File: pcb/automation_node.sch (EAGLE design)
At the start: 27 parts, among them IC1 POWER_FET, IC2 POWER_FET, IC3 POWER_FET, IC4 POWER_FET, IC5 POWER_FET, IC6 FEATHER-ESP32, J1 POWER-VIAS, J2 POWER-VIAS, J3 POWER-VIAS, J4 POWER-VIAS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

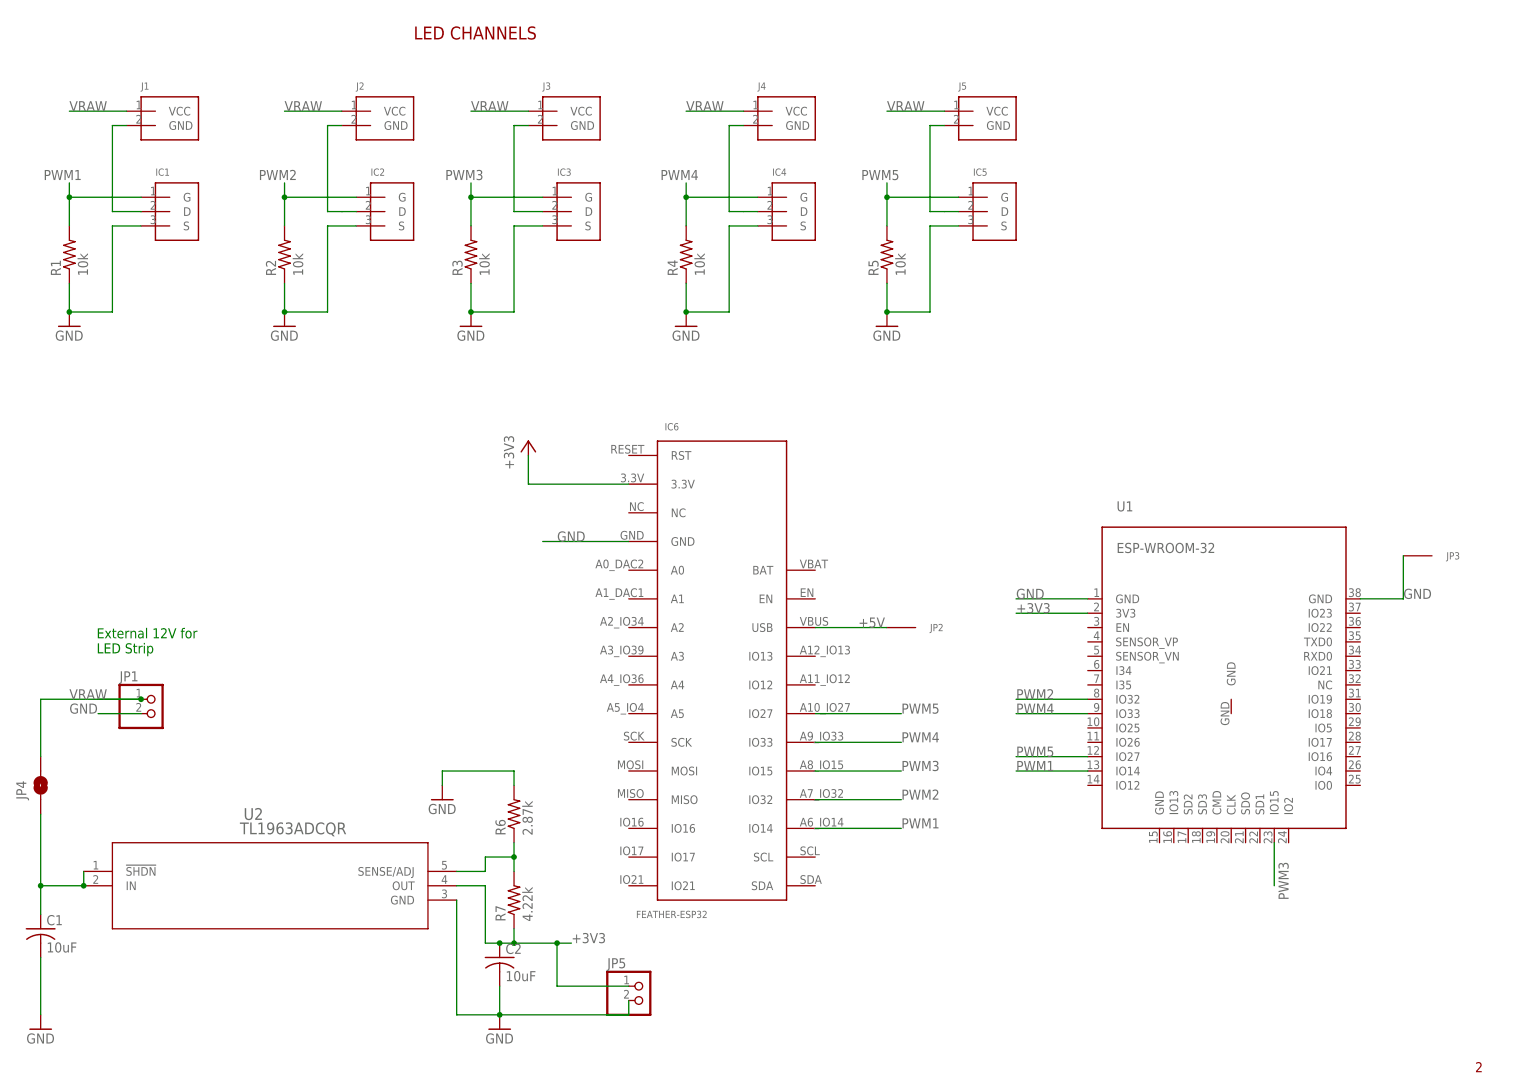
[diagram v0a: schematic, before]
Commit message: added RFM69, finished routing all but RFM69
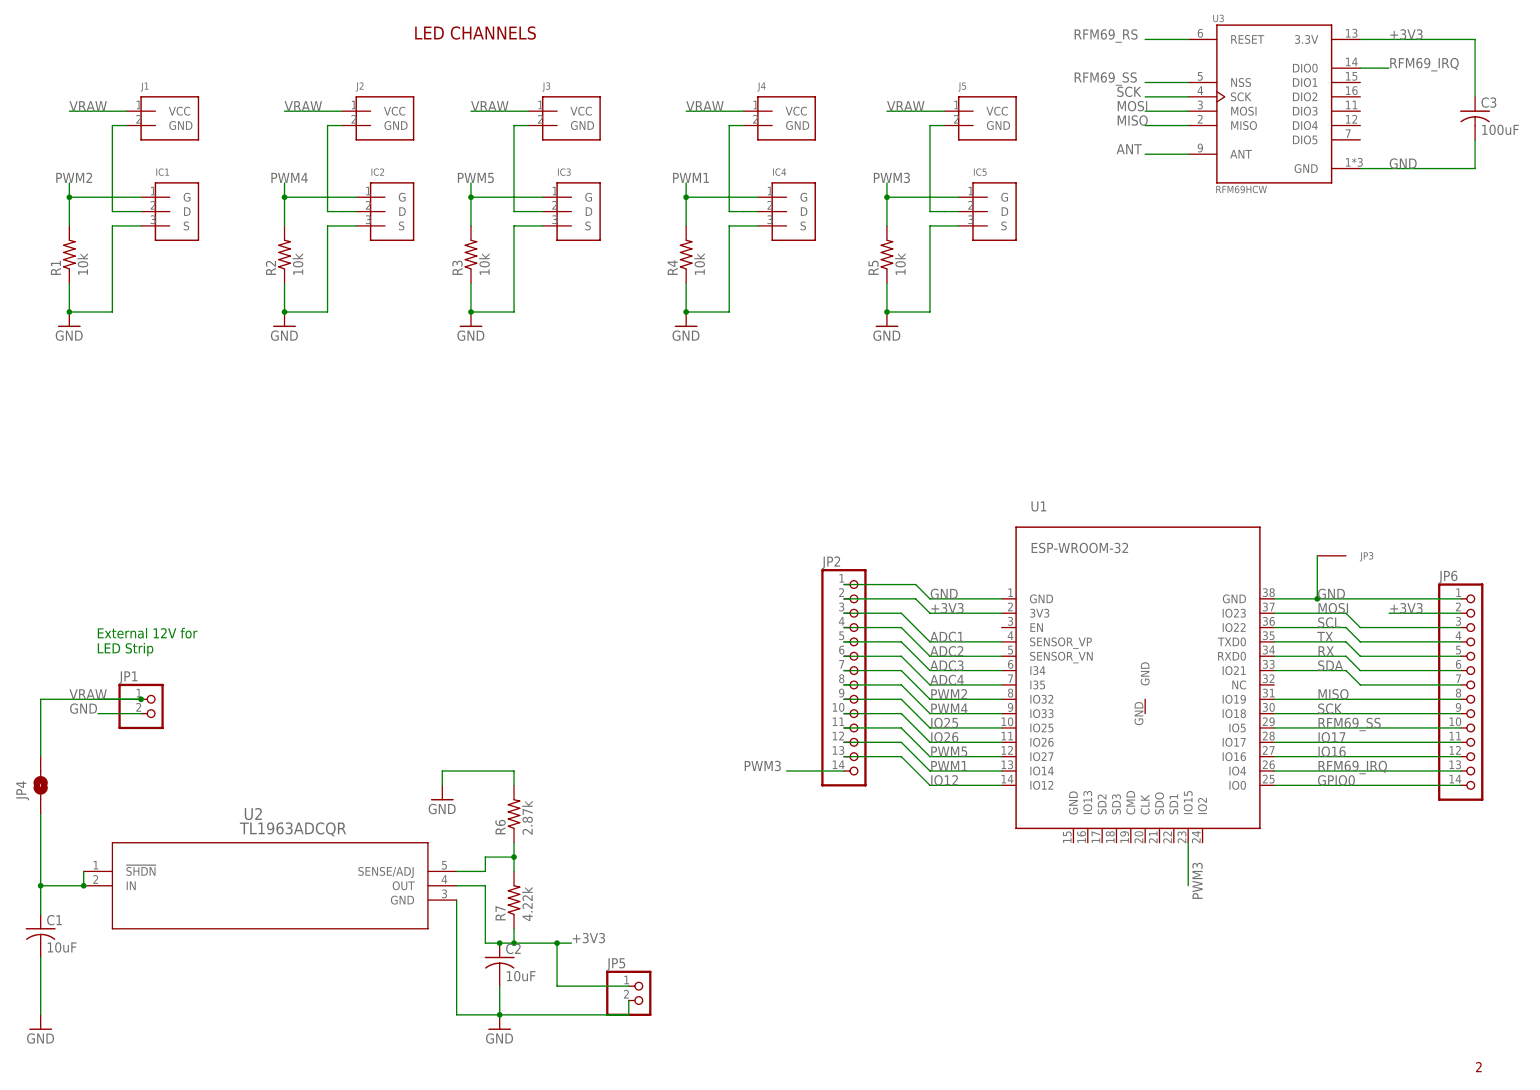
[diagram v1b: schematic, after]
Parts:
- removed IC6: FEATHER-ESP32, VCO-Eagle_parts:FEATHER-ESP32
- added C3: 100uF, rcl:C-USC0805
- added JP6: (no value), pinhead:PINHD-1X14
- added U3: RFM69HCW, VanEagleLib:RFM69HCW
- JP2: value PROTO_VIA_COMPACT -> (none); device VanEagleLib:PROTO_VIA_COMPACT -> pinhead:PINHD-1X14
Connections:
- removed net +5V: IC6.USB, JP2.1
- new net ADC1: JP2.3, U1.SENSOR_VP
- new net ADC2: JP2.4, U1.SENSOR_VN
- new net ADC3: JP2.5, U1.I34
- new net ADC4: JP2.6, U1.I35
- new net ANT: U3.ANT
- new net GPIO0: JP6.14, U1.IO0
- new net IO12: JP2.13, U1.IO12
- new net IO16: JP6.12, U1.IO16
- new net IO17: JP6.11, U1.IO17
- new net IO25: JP2.9, U1.IO25
- new net IO26: JP2.10, U1.IO26
- new net MISO: JP6.8, U1.IO19, U3.MISO
- new net MOSI: JP6.3, U1.IO23, U3.MOSI
- new net RFM69_IRQ: JP6.13, U1.IO4, U3.DIO0
- new net RFM69_RS: U3.RESET
- new net RFM69_SS: JP6.10, U1.IO5, U3.NSS
- new net RX: JP6.6, U1.RXD0
- new net SCK: JP6.9, U1.IO18, U3.SCK
- new net SCL: JP6.4, U1.IO22
- new net SDA: JP6.7, U1.IO21
- new net TX: JP6.5, U1.TXD0
- net +3V3: now also C3.1, JP2.2, JP6.2, U3.3.3V; no longer IC6.3.3V
- net GND: now also C3.2, JP2.1, JP6.1, U3.GND; no longer IC6.GND
- net PWM1: now also IC4.G, JP2.12, R4.2; no longer IC1.G, IC6.IO14, R1.2
- net PWM2: now also IC1.G, JP2.7, R1.2; no longer IC2.G, IC6.IO32, R2.2
- net PWM3: now also IC5.G, JP2.14, R5.2; no longer IC3.G, IC6.IO15, R3.2
- net PWM4: now also IC2.G, JP2.8, R2.2; no longer IC4.G, IC6.IO33, R4.2
- net PWM5: now also IC3.G, JP2.11, R3.2; no longer IC5.G, IC6.IO27, R5.2
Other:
- moved on the sheet: JP3, U1

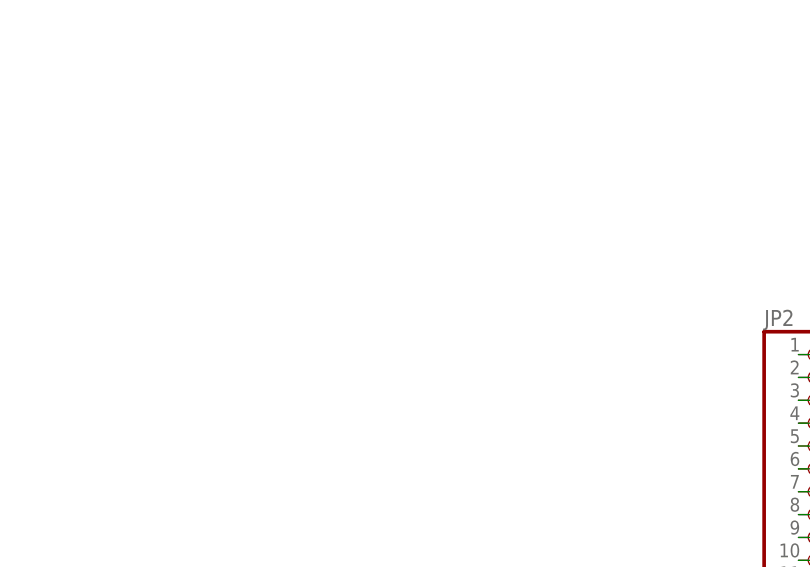
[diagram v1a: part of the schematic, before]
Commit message: added programming header for ESP32
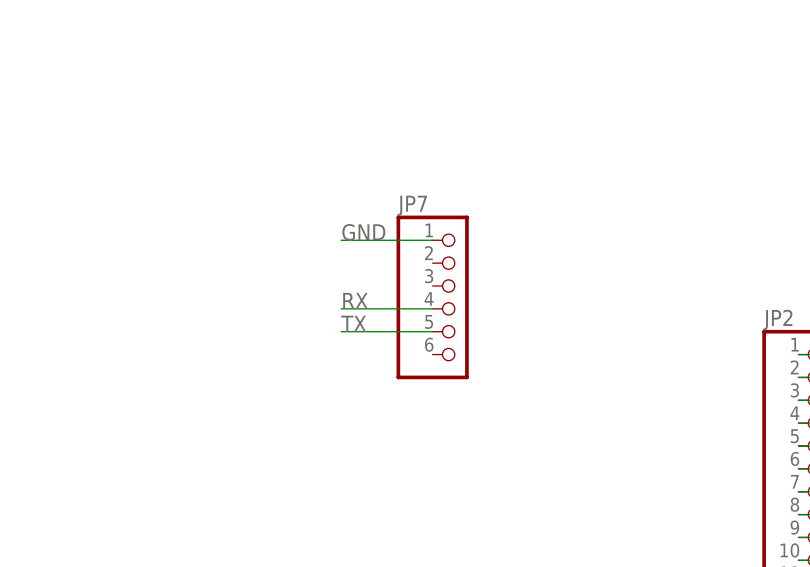
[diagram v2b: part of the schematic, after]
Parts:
- added JP7: (no value), pinhead:PINHD-1X6
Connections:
- net GND: now also JP7.1
- net RX: now also JP7.4
- net TX: now also JP7.5
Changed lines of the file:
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@@
 <part name="JP2" library="pinhead" library_urn="urn:adsk.eagle:library:325" deviceset="PINHD-1X14" device="" package3d_urn="urn:adsk.eagle:package:22417/2"/>
 <part name="JP6" library="pinhead" library_urn="urn:adsk.eagle:library:325" deviceset="PINHD-1X14" device="" package3d_urn="urn:adsk.eagle:package:22417/2"/>
+<part name="JP7" library="pinhead" library_urn="urn:adsk.eagle:library:325" deviceset="PINHD-1X6" device="" package3d_urn="urn:adsk.eagle:package:22472/2"/>
 </parts>
 <sheets>
@@
 <attribute name="VALUE" x="260.35" y="53.34" size="1.778" layer="96"/>
 </instance>
+<instance part="JP7" gate="A" x="116.84" y="99.06" smashed="yes">
+<attribute name="NAME" x="110.49" y="109.855" size="1.778" layer="95"/>
+<attribute name="VALUE" x="110.49" y="88.9" size="1.778" layer="96"/>
+</instance>
 </instances>
 <busses>
@@
 <wire x1="266.7" y1="172.72" x2="266.7" y2="167.64" width="0.1524" layer="91"/>
 <wire x1="266.7" y1="167.64" x2="246.38" y2="167.64" width="0.1524" layer="91"/>
+</segment>
+<segment>
+<pinref part="JP7" gate="A" pin="1"/>
+<wire x1="114.3" y1="106.68" x2="104.14" y2="106.68" width="0.1524" layer="91"/>
+<label x="104.14" y="106.68" size="1.778" layer="95"/>
 </segment>
 </net>
@@
 <wire x1="246.38" y1="81.28" x2="264.16" y2="81.28" width="0.1524" layer="91"/>
 </segment>
+<segment>
+<pinref part="JP7" gate="A" pin="5"/>
+<wire x1="114.3" y1="96.52" x2="104.14" y2="96.52" width="0.1524" layer="91"/>
+<label x="104.14" y="96.52" size="1.778" layer="95"/>
+</segment>
 </net>
 <net name="RX" class="0">
@@
 <wire x1="246.38" y1="78.74" x2="264.16" y2="78.74" width="0.1524" layer="91"/>
 </segment>
-</net>
+<segment>
+<pinref part="JP7" gate="A" pin="4"/>
+<wire x1="114.3" y1="99.06" x2="104.14" y2="99.06" width="0.1524" layer="91"/>
+<label x="104.14" y="99.06" size="1.778" layer="95"/>
+</segment>
+</net>

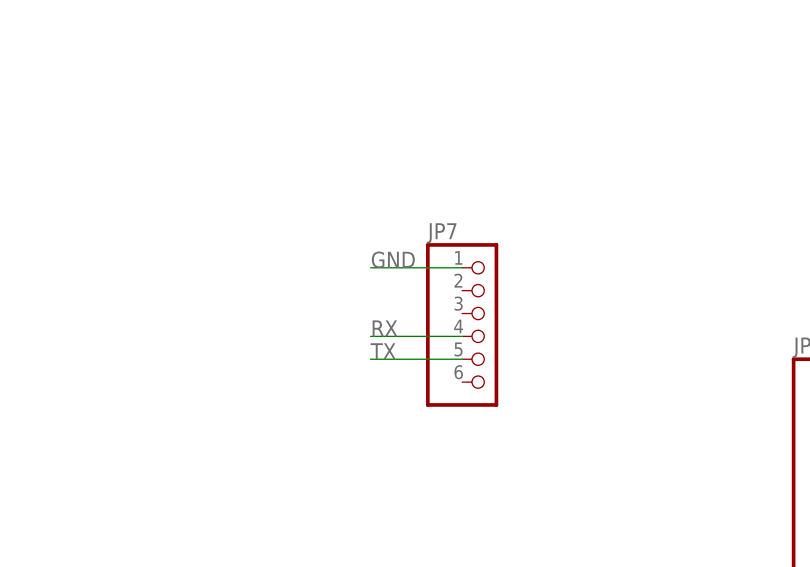
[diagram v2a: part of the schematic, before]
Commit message: added GPIO0 to programming header
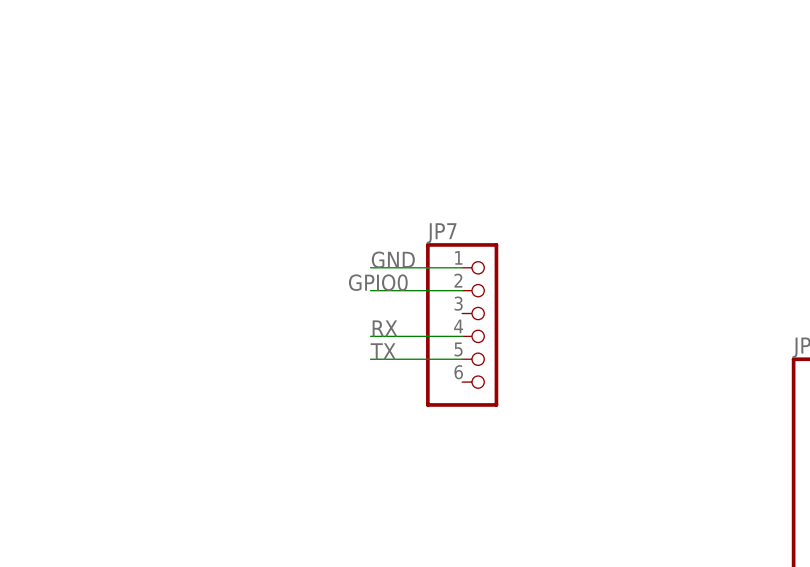
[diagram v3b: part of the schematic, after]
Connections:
- net GPIO0: now also JP7.2
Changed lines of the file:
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@@
 <wire x1="231.14" y1="58.42" x2="264.16" y2="58.42" width="0.1524" layer="91"/>
+</segment>
+<segment>
+<pinref part="JP7" gate="A" pin="2"/>
+<wire x1="114.3" y1="104.14" x2="104.14" y2="104.14" width="0.1524" layer="91"/>
+<label x="101.6" y="104.14" size="1.778" layer="95"/>
 </segment>
 </net>
